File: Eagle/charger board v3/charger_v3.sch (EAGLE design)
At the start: 32 parts, among them IC1 IR2110D, Q1 2N7000, Q2 IRFP240, Q3 MJE13003G

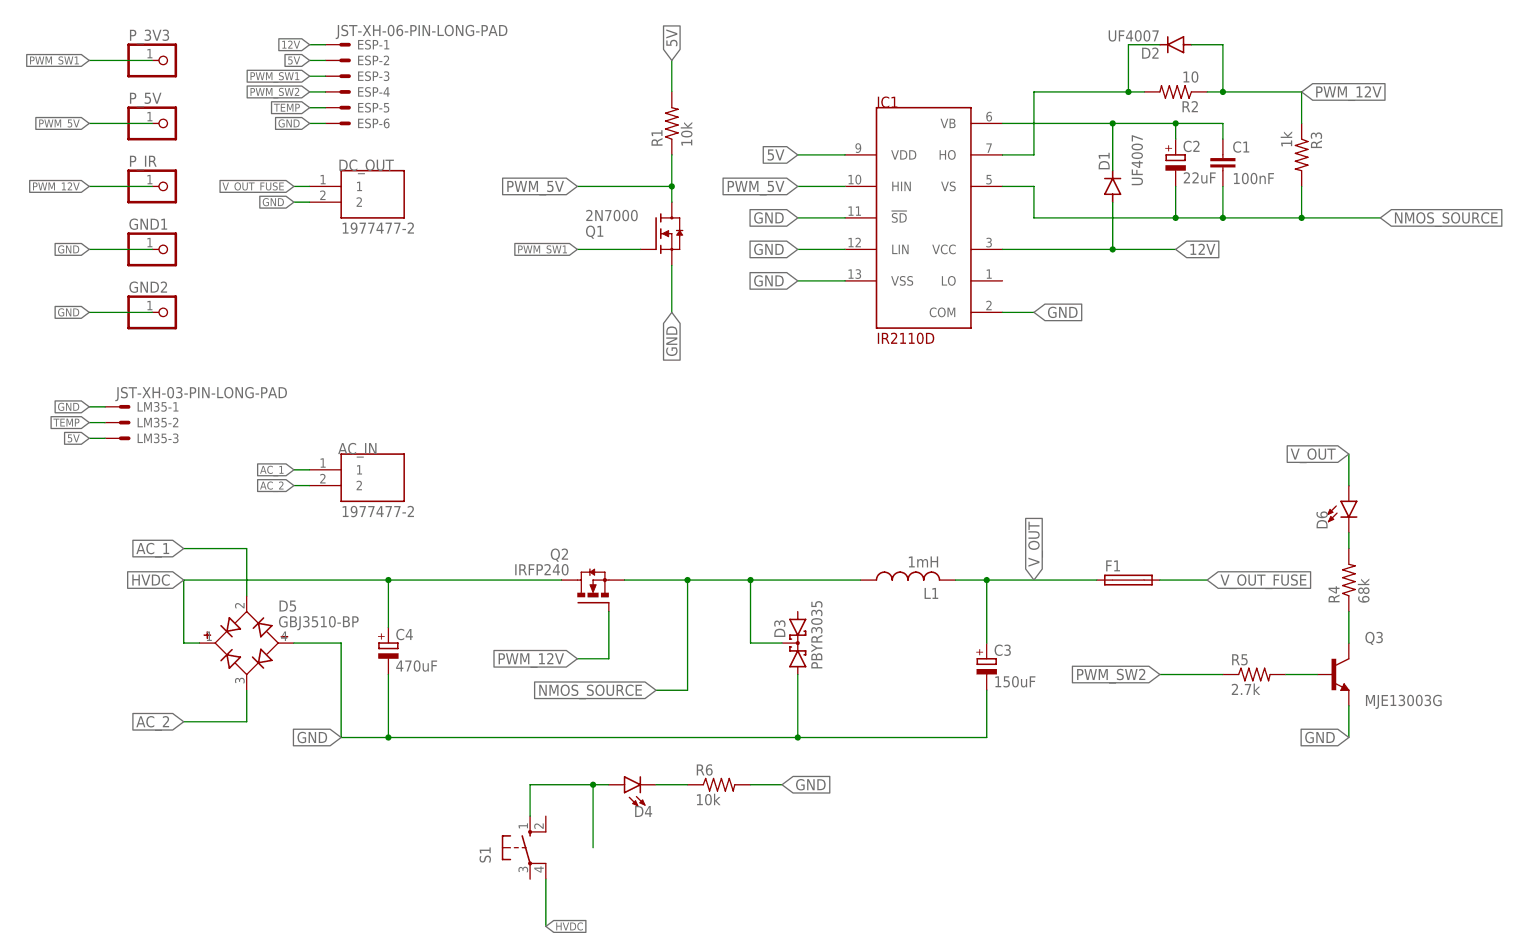
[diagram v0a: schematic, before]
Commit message: ubah 2n700 ke opto + nambahin snubber di mosfet sama dioda
ubah 2n700 ke opto + nambahin snubber di mosfet sama dioda
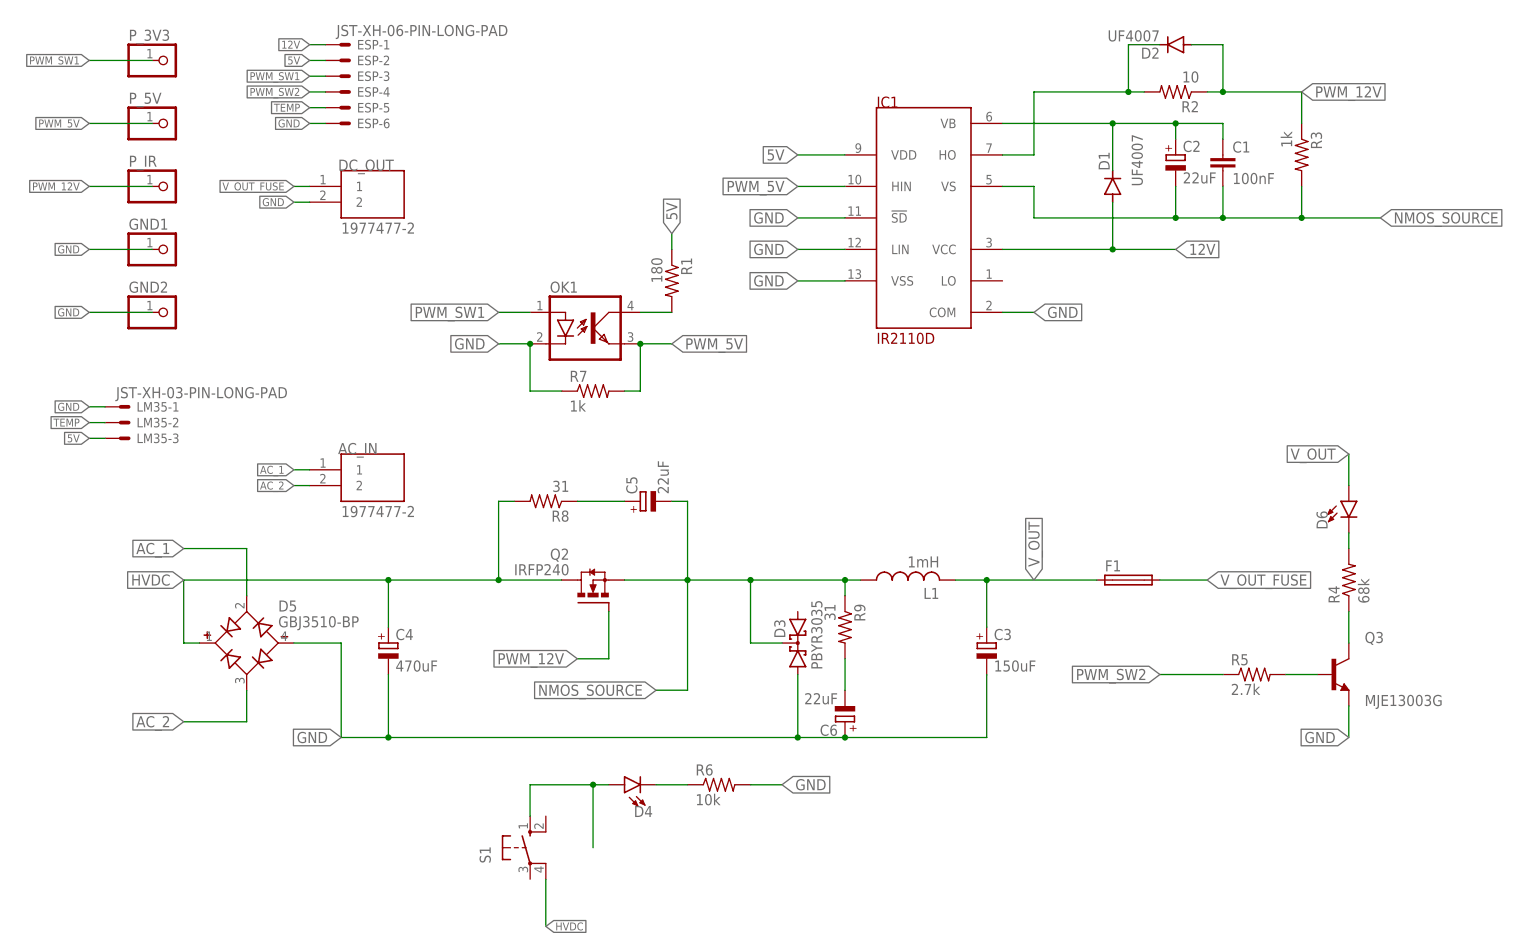
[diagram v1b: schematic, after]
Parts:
- removed Q1: 2N7000, 2N7000:2N7000
- added C5, C6: 22uF, rcl:CPOL-EUE7.5-18
- added OK1: SFH618A-5, optocoupler:SFH618A-5
- added R7: 1k, rcl:R-US_0204/7
- added R8, R9: 31, rcl:R-US_0411/15
- R1: value 10k -> 180
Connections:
- new net N$11: OK1.COL, R1.2
- new net N$6: C5.+, R8.1
- new net N$7: C6.-, R9.2
- net 5V: now also R1.1; no longer R1.2
- net GND: now also C6.+, OK1.C, R7.1; no longer Q1.S
- net HVDC: now also R8.2
- net NMOS_SOURCE: now also C5.-, R9.1
- net PWM_5V: now also OK1.EMIT, R7.2; no longer Q1.D, R1.1
- net PWM_SW1: now also OK1.A; no longer Q1.G
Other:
- moved on the sheet: C3, R1
